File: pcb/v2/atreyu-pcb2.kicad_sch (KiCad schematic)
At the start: 129 parts, among them J1 OLED, J2 Conn_01x02_Female, SW1 SW_Push, SW2 RotaryEncoder_Switch, SW3 RotaryEncoder_Switch, SW4 SW_SPDT, U1 Elite-C

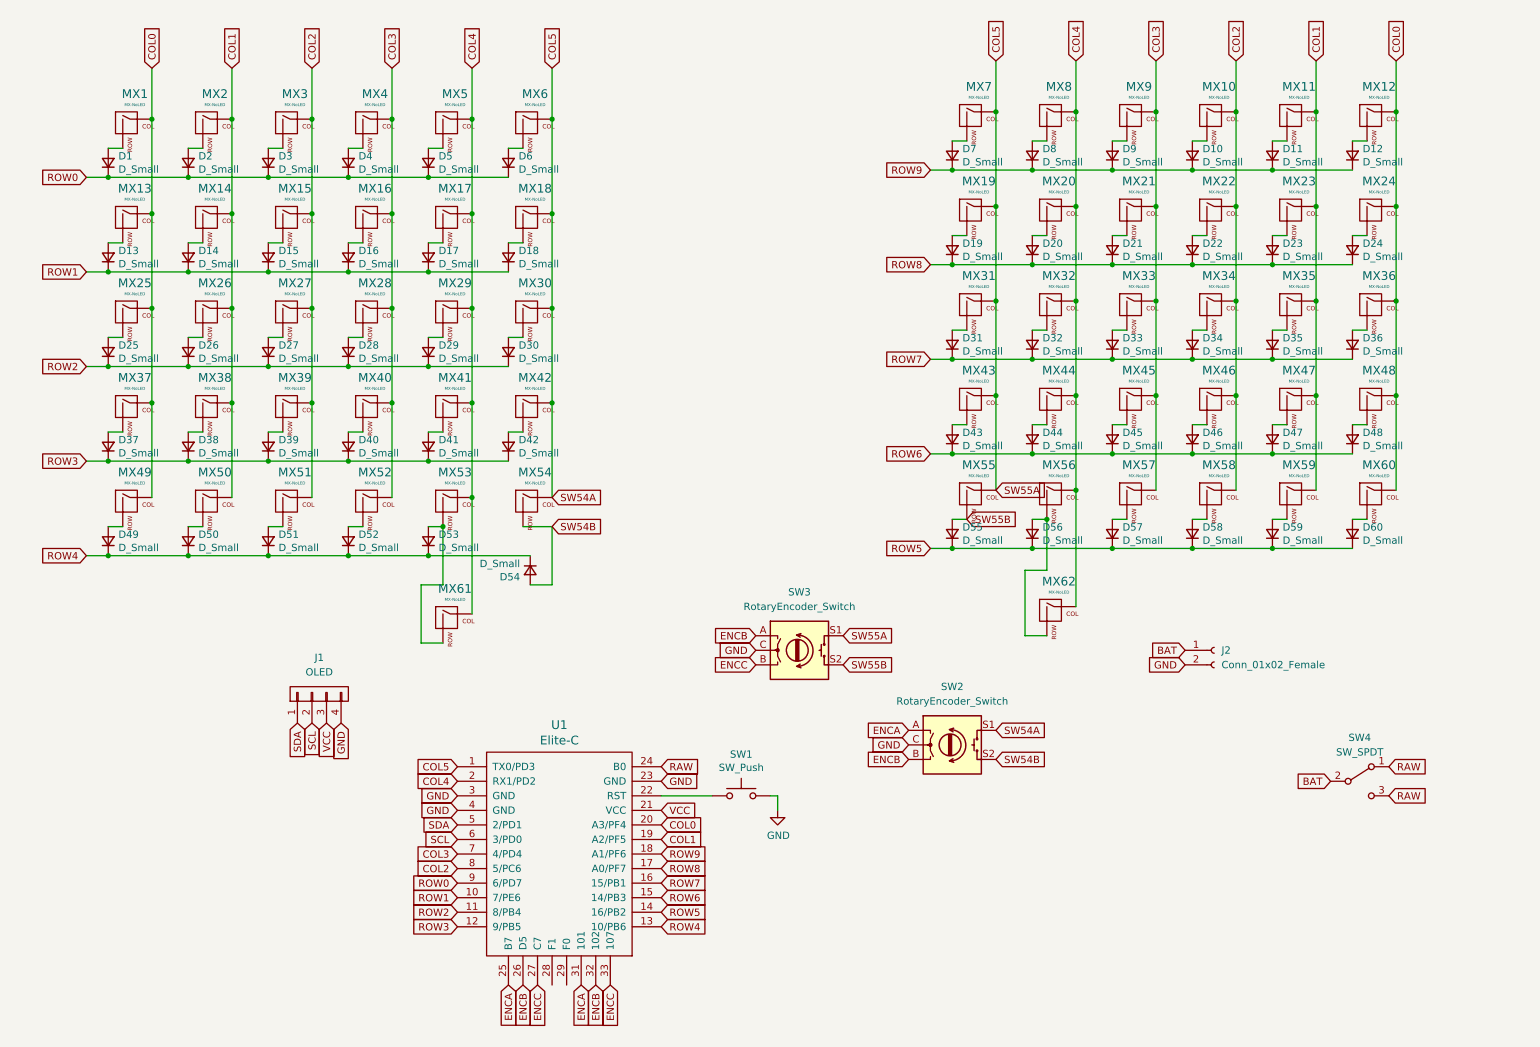
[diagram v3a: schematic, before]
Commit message: Updated routing, added LED option.
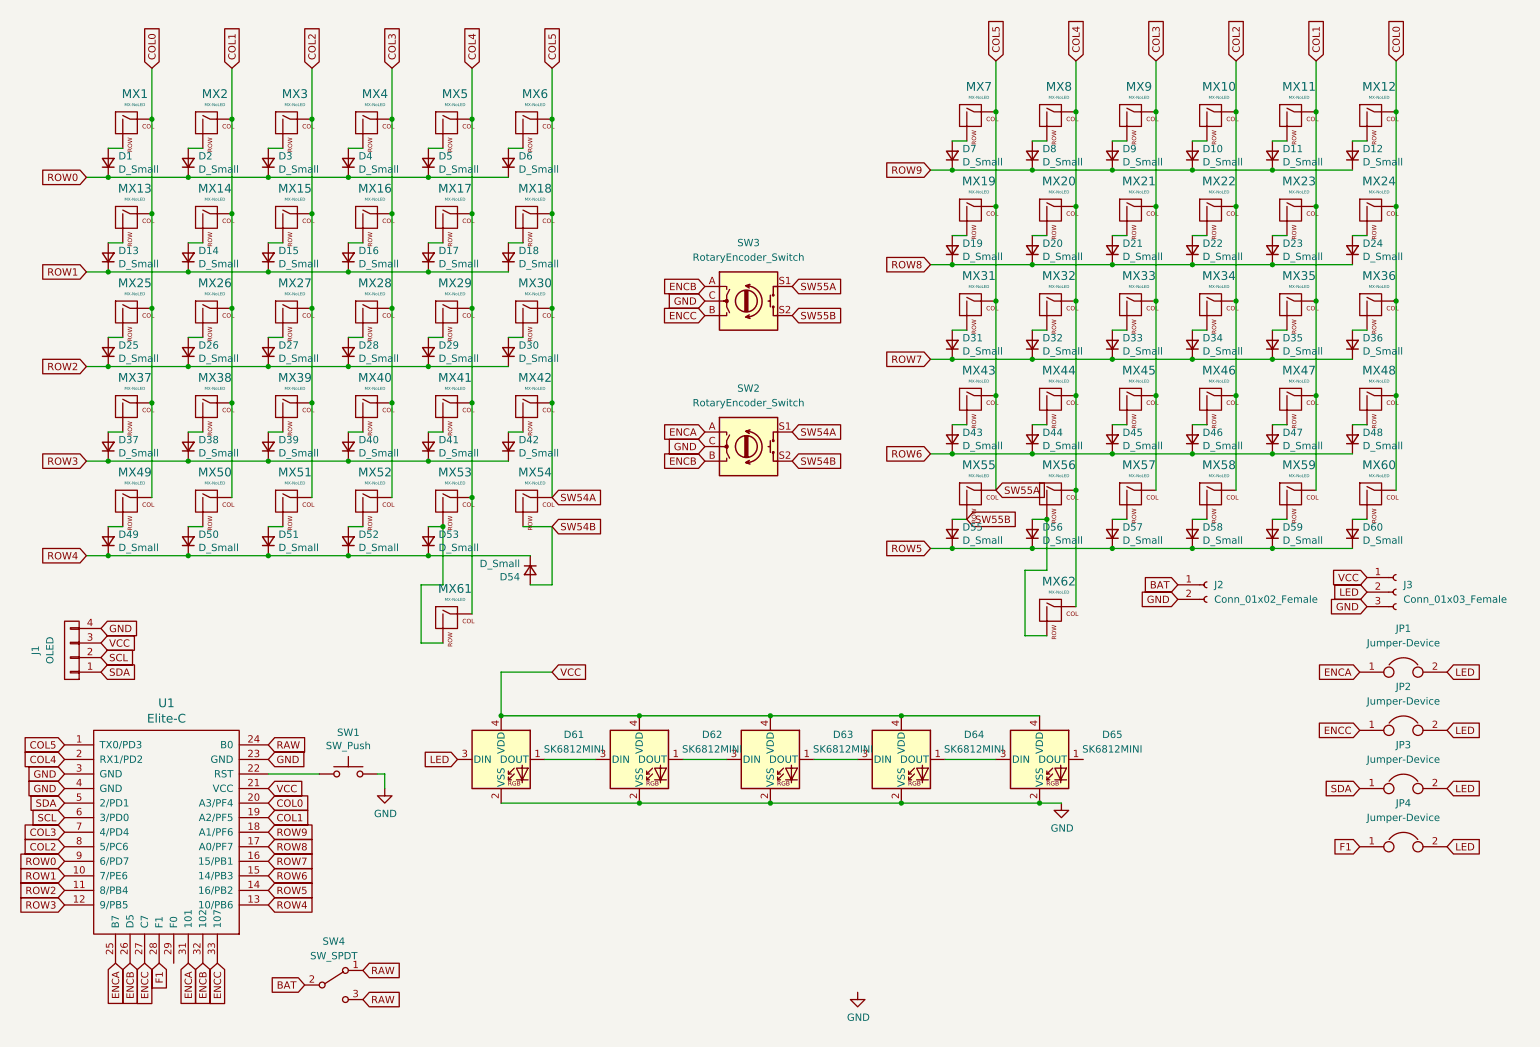
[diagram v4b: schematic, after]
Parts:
- added D61, D62, D63, D64, D65: SK6812MINI, footprints:YS-SK6812MINI-E, symbol LED:SK6812MINI
- added J3: Conn_01x03_Female, Connector_PinHeader_2.54mm:PinHeader_1x03_P2.54mm_Vertical, symbol Connector:Conn_01x03_Female
- added JP1, JP2, JP3, JP4: Jumper-Device, Jumper:SolderJumper-2_P1.3mm_Open_RoundedPad1.0x1.5mm, symbol SouffleKeyboard-rescue:Jumper-Device
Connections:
- net ENCA: now also JP1.1
- net ENCC: now also JP2.1
- net GND: now also D61.2 (VSS), D62.2 (VSS), D63.2 (VSS), D64.2 (VSS), D65.2 (VSS), J3.3 (Pin_3)
- net SDA: now also JP3.1
- net VCC: now also D61.4 (VDD), D62.4 (VDD), D63.4 (VDD), D64.4 (VDD), D65.4 (VDD), J3.1 (Pin_1)
- net F1: now reaches U1.28 (F1)
- net F1: now also JP4.1
- new net: D61.1 (DOUT), D62.3 (DIN)
- new net: D62.1 (DOUT), D63.3 (DIN)
- new net: D64.1 (DOUT), D65.3 (DIN)
- new net: D63.1 (DOUT), D64.3 (DIN)
- new net LED: D61.3 (DIN), J3.2 (Pin_2), JP1.2, JP2.2, JP3.2, JP4.2
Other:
- moved on the sheet: J1, J2, SW1, SW2, SW3, SW4, U1

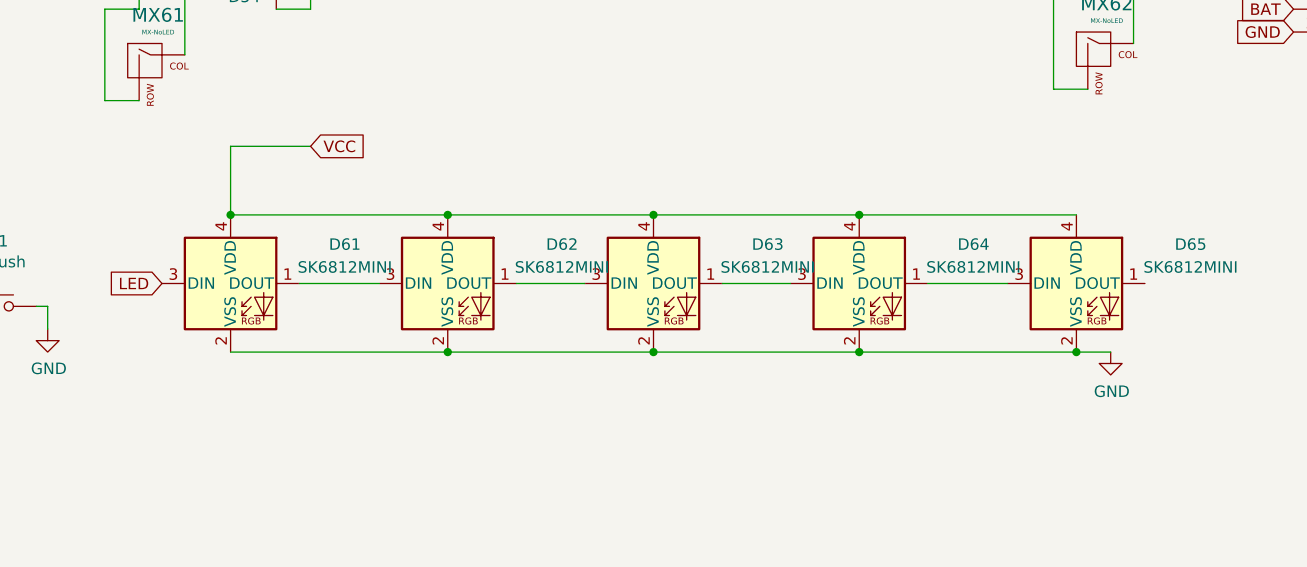
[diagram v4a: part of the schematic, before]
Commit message: Fixed v2.0.1 Atreyu with mini-e schematics.
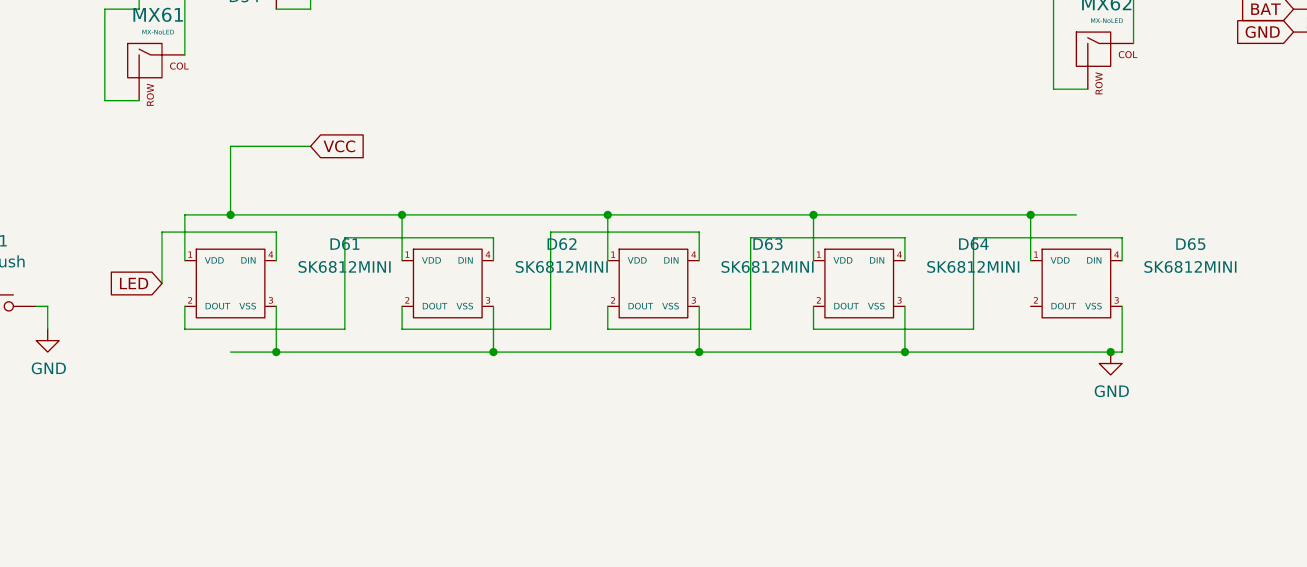
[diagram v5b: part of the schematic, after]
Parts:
- D61, D62, D63, D64, D65: symbol LED:SK6812MINI -> atreyu-pcb2:SK6812MINI_LED
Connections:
- net GND: now also D61.3 (VSS), D62.3 (VSS), D63.3 (VSS), D64.3 (VSS), D65.3 (VSS); no longer D61.2 (VSS), D62.2 (VSS), D63.2 (VSS), D64.2 (VSS), D65.2 (VSS)
- net LED: now also D61.4 (DIN); no longer D61.3 (DIN)
- net VCC: now also D61.1 (VDD), D62.1 (VDD), D63.1 (VDD), D64.1 (VDD), D65.1 (VDD); no longer D61.4 (VDD), D62.4 (VDD), D63.4 (VDD), D64.4 (VDD), D65.4 (VDD)
- new net: D61.2 (DOUT), D62.4 (DIN)
- new net: D62.2 (DOUT), D63.4 (DIN)
- new net: D64.2 (DOUT), D65.4 (DIN)
- new net: D63.2 (DOUT), D64.4 (DIN)
